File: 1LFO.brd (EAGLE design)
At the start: 96.8 x 17.8 mm, 26 parts, among them IC1 LM324D

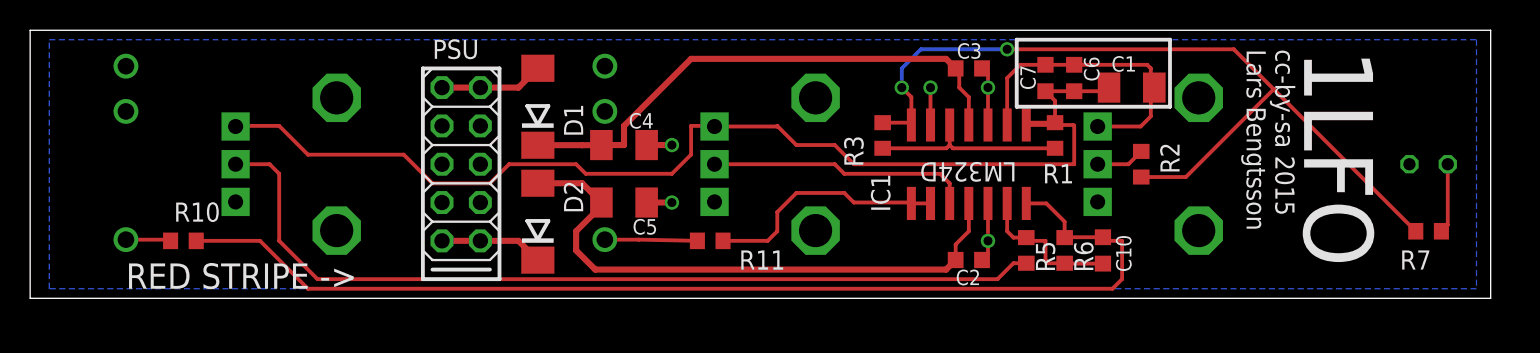
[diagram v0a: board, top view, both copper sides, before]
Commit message: Moved LED 2.54mm up, fits panel now (originally a mistake, but panel looks fine now. Better fix board). Also, size down other end of PCB to save a few cents on manufacturing.
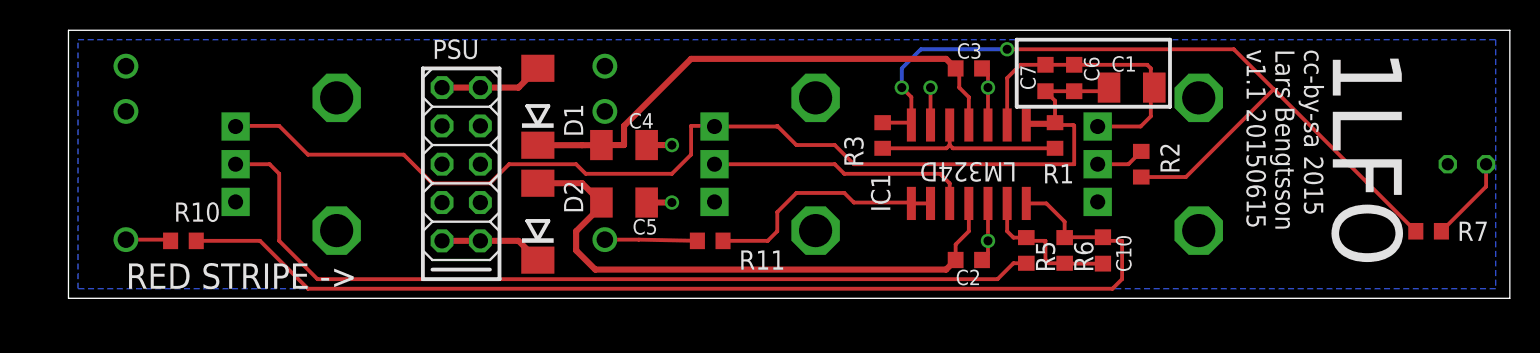
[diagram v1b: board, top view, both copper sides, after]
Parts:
- LED1: device led:LED5MM -> led:LED3MM
- moved LED1 2.54 mm to (96.5, 10.2)
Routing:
- net N$13: track 4.62 -> 5.67 mm
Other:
- board size 96.8 x 17.8 mm -> 95.6 x 17.8 mm
- board text added: "cc-by-sa 2015 Lars Bengtsson v1.1 20150615"
- board text removed: "cc-by-sa 2015 Lars Bengtsson"
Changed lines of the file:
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@@
 <board>
 <plain>
-<wire x1="1.27" y1="1.27" x2="98.095" y2="1.27" width="0" layer="20"/>
-<wire x1="98.095" y1="1.27" x2="98.095" y2="19.04" width="0" layer="20"/>
-<wire x1="98.095" y1="19.04" x2="1.27" y2="19.04" width="0" layer="20"/>
-<wire x1="1.27" y1="19.04" x2="1.27" y2="1.27" width="0" layer="20"/>
+<wire x1="3.81" y1="1.27" x2="99.365" y2="1.27" width="0" layer="20"/>
+<wire x1="99.365" y1="1.27" x2="99.365" y2="19.04" width="0" layer="20"/>
+<wire x1="99.365" y1="19.04" x2="3.81" y2="19.04" width="0" layer="20"/>
+<wire x1="3.81" y1="19.04" x2="3.81" y2="1.27" width="0" layer="20"/>
 <wire x1="27.305" y1="16.51" x2="27.305" y2="2.54" width="0.254" layer="25"/>
 <wire x1="27.305" y1="2.54" x2="32.385" y2="2.54" width="0.254" layer="25"/>
@@
 <wire x1="27.305" y1="16.51" x2="32.385" y2="16.51" width="0.254" layer="25"/>
 <text x="7.62" y="1.905" size="1.6764" layer="25" font="vector">RED STRIPE -&gt;</text>
-<text x="85.725" y="17.78" size="4.572" layer="25" font="vector" rot="SR270">1LFO</text>
+<text x="87.63" y="17.78" size="4.572" layer="25" font="vector" rot="SR270">1LFO</text>
 <text x="81.915" y="17.78" size="1.27" layer="25" font="vector" rot="SR270">cc-by-sa 2015
-Lars Bengtsson</text>
+Lars Bengtsson
+v1.1 20150615</text>
 <wire x1="66.675" y1="18.415" x2="66.675" y2="13.97" width="0.254" layer="25"/>
 <wire x1="66.675" y1="13.97" x2="76.835" y2="13.97" width="0.254" layer="25"/>
@@
 <element name="INV.AM." library="pot-alps" package="ALPS_POT_VERTICAL" value="100k" x="21.59" y="10.16" rot="MR270"/>
 <element name="OUT" library="thonkiconn" package="WQP-PJ301M-12_JACK" value="WQP-PJ301M-12_JACK" x="39.37" y="10.16" rot="MR180"/>
-<element name="INV_OUT" library="thonkiconn" package="WQP-PJ301M-12_JACK" value="WQP-PJ301M-12_JACK" x="7.62" y="10.16" rot="MR180"/>
+<element name="INV_OUT" library="thonkiconn" package="WQP-PJ301M-12_JACK" value="WQP-PJ301M-12_JACK" x="7.62" y="10.16" smashed="yes" rot="MR180">
+<attribute name="NAME" x="13.6652" y="17.1704" size="1.27" layer="22" rot="MR270"/>
+</element>
 <element name="R7" library="rcl" package="R0603" value="10k" x="93.98" y="5.715" smashed="yes">
-<attribute name="NAME" x="92.075" y="3.175" size="1.27" layer="25"/>
-<attribute name="VALUE" x="94.615" y="3.175" size="1.27" layer="27"/>
-</element>
-<element name="LED1" library="led" package="LED5MM" value="" x="93.98" y="10.16" smashed="yes" rot="MR0">
-<attribute name="NAME" x="96.52" y="13.8684" size="1.27" layer="26" ratio="10" rot="MR0"/>
-<attribute name="VALUE" x="90.7796" y="8.3566" size="1.27" layer="28" ratio="10" rot="MR0"/>
+<attribute name="NAME" x="95.885" y="5.08" size="1.27" layer="25"/>
+<attribute name="VALUE" x="95.885" y="3.175" size="1.27" layer="27"/>
+</element>
+<element name="LED1" library="led" package="LED3MM" value="" x="96.52" y="10.16" smashed="yes" rot="MR0">
+<attribute name="NAME" x="97.79" y="13.2334" size="1.27" layer="26" ratio="10" rot="MR0"/>
+<attribute name="VALUE" x="93.3196" y="8.3566" size="1.27" layer="28" ratio="10" rot="MR0"/>
 </element>
 </elements>
@@
 <contactref element="LED1" pad="K"/>
 <polygon width="0.254" layer="16" isolate="0.3048">
-<vertex x="2.54" y="18.415"/>
-<vertex x="97.155" y="18.415"/>
-<vertex x="97.155" y="1.905"/>
-<vertex x="2.54" y="1.905"/>
+<vertex x="4.445" y="18.415"/>
+<vertex x="98.425" y="18.415"/>
+<vertex x="98.425" y="1.905"/>
+<vertex x="4.445" y="1.905"/>
 </polygon>
 <wire x1="64.77" y1="12.76" x2="64.77" y2="12.7" width="0.254" layer="1"/>
@@
 <contactref element="R7" pad="2"/>
 <contactref element="LED1" pad="A"/>
-<wire x1="95.25" y1="10.16" x2="95.25" y2="6.135" width="0.254" layer="1"/>
-<wire x1="95.25" y1="6.135" x2="94.83" y2="5.715" width="0.254" layer="1"/>
+<wire x1="97.79" y1="10.16" x2="97.79" y2="8.675" width="0.254" layer="1"/>
+<wire x1="97.79" y1="8.675" x2="94.83" y2="5.715" width="0.254" layer="1"/>
 </signal>
 </signals>

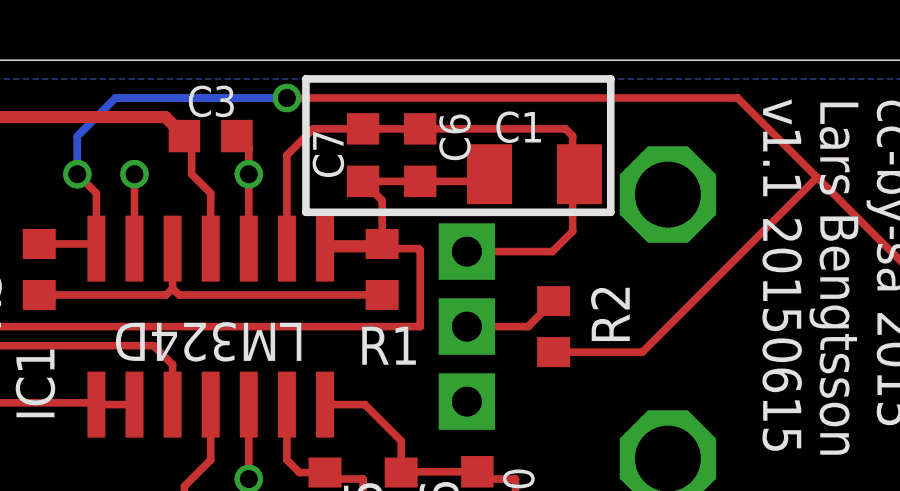
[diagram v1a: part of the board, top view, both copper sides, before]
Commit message: Removed C7. Moved remaining timing caps a bit and changed value to the right one (10uF). Only one of C1 and C6 needs to be fitted. 10uF caps are easier to find in 1206 packages with higher voltage tolerances (should be >= 16V).
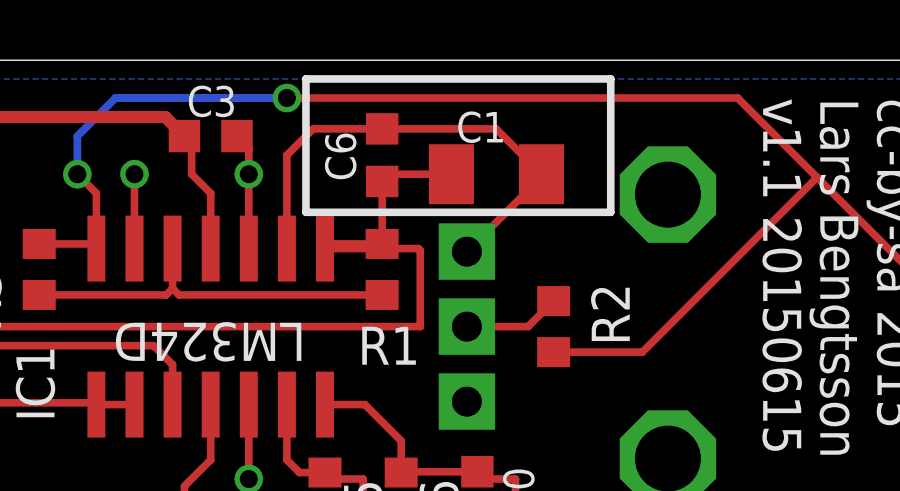
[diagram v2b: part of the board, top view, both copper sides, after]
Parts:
- removed C7: 1u, rcl:C0603K
- C1, C6: value 1u -> 10u
- moved C1 1.27 mm to (73.0, 15.2)
- moved C6 1.27 mm to (69.2, 15.9)
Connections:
- net N$1: no longer C7.1
- net TRI: no longer C7.2
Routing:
- net N$1: track 20.3 -> 16.2 mm
- net TRI: track 75.9 -> 73.7 mm
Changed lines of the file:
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@@
 </autorouter>
 <elements>
-<element name="C1" library="rcl" package="C1206K" value="1u" x="74.295" y="15.24" smashed="yes" rot="R180">
-<attribute name="NAME" x="74.625" y="17.315" size="1.016" layer="25" rot="R180"/>
+<element name="C1" library="rcl" package="C1206K" value="10u" x="73.025" y="15.24" smashed="yes" rot="R180">
+<attribute name="NAME" x="73.355" y="17.315" size="1.016" layer="25" rot="R180"/>
 <attribute name="VALUE" x="76.53" y="17.34" size="1.016" layer="27" rot="R180"/>
 </element>
@@
 <attribute name="VALUE" x="42.875" y="5.275" size="1.016" layer="27" rot="R180"/>
 </element>
-<element name="C6" library="rcl" package="C0603K" value="1u" x="70.485" y="15.875" smashed="yes" rot="R270">
-<attribute name="NAME" x="71.135" y="17.31" size="1.016" layer="25" rot="R270"/>
-<attribute name="VALUE" x="70.32" y="17.4" size="1.016" layer="27"/>
-</element>
-<element name="C7" library="rcl" package="C0603K" value="1u" x="68.58" y="15.875" smashed="yes" rot="R270">
-<attribute name="NAME" x="67.93" y="15.075" size="1.016" layer="25" rot="R90"/>
+<element name="C6" library="rcl" package="C0603K" value="10u" x="69.215" y="15.875" smashed="yes" rot="R270">
+<attribute name="NAME" x="67.325" y="16.675" size="1.016" layer="25" rot="R270"/>
 <attribute name="VALUE" x="67.78" y="17.4" size="1.016" layer="27"/>
 </element>
@@
 <contactref element="C1" pad="1"/>
 <contactref element="C6" pad="1"/>
-<contactref element="C7" pad="1"/>
-<wire x1="68.58" y1="16.75" x2="70.485" y2="16.75" width="0.254" layer="1"/>
-<wire x1="68.58" y1="16.75" x2="66.915" y2="16.75" width="0.254" layer="1"/>
 <wire x1="66.915" y1="16.75" x2="66.04" y2="15.875" width="0.254" layer="1"/>
 <wire x1="66.04" y1="15.875" x2="66.04" y2="12.76" width="0.254" layer="1"/>
-<wire x1="70.485" y1="16.75" x2="75.325" y2="16.75" width="0.254" layer="1"/>
-<wire x1="75.325" y1="16.75" x2="75.565" y2="16.51" width="0.254" layer="1"/>
-<wire x1="75.565" y1="16.51" x2="75.565" y2="15.47" width="0.254" layer="1"/>
-<wire x1="75.565" y1="15.47" x2="75.795" y2="15.24" width="0.254" layer="1"/>
-<wire x1="72.04" y1="12.66" x2="74.89" y2="12.66" width="0.254" layer="1"/>
-<wire x1="74.89" y1="12.66" x2="75.565" y2="13.335" width="0.254" layer="1"/>
-<wire x1="75.565" y1="13.335" x2="75.565" y2="15.01" width="0.254" layer="1"/>
-<wire x1="75.565" y1="15.01" x2="75.795" y2="15.24" width="0.254" layer="1"/>
+<wire x1="66.915" y1="16.75" x2="69.215" y2="16.75" width="0.254" layer="1"/>
+<wire x1="69.215" y1="16.75" x2="73.015" y2="16.75" width="0.254" layer="1"/>
+<wire x1="73.015" y1="16.75" x2="74.525" y2="15.24" width="0.254" layer="1"/>
+<wire x1="74.525" y1="15.24" x2="74.525" y2="15.145" width="0.254" layer="1"/>
+<wire x1="74.525" y1="15.145" x2="72.04" y2="12.66" width="0.254" layer="1"/>
 </signal>
 <signal name="TRI">
@@
 <contactref element="C1" pad="2"/>
 <contactref element="C6" pad="2"/>
-<contactref element="C7" pad="2"/>
 <contactref element="AM." pad="P$1"/>
 <contactref element="INV.AM." pad="P$1"/>
 <wire x1="69.215" y1="12.915" x2="67.465" y2="12.915" width="0.254" layer="1"/>
 <wire x1="67.465" y1="12.915" x2="67.31" y2="12.76" width="0.254" layer="1"/>
-<wire x1="69.215" y1="12.915" x2="69.215" y2="14.365" width="0.254" layer="1"/>
-<wire x1="69.215" y1="14.365" x2="68.58" y2="15" width="0.254" layer="1"/>
-<wire x1="68.58" y1="15" x2="70.485" y2="15" width="0.254" layer="1"/>
-<wire x1="70.485" y1="15" x2="72.555" y2="15" width="0.254" layer="1"/>
-<wire x1="72.555" y1="15" x2="72.795" y2="15.24" width="0.254" layer="1"/>
+<wire x1="69.215" y1="12.915" x2="69.215" y2="15" width="0.254" layer="1"/>
 <wire x1="67.31" y1="12.76" x2="70.425" y2="12.76" width="0.254" layer="1"/>
 <wire x1="70.425" y1="12.76" x2="70.485" y2="12.7" width="0.254" layer="1"/>
@@
 <wire x1="50.8" y1="12.7" x2="52.07" y2="11.43" width="0.254" layer="1"/>
 <wire x1="52.07" y1="11.43" x2="54.61" y2="11.43" width="0.254" layer="1"/>
+<wire x1="71.525" y1="15.24" x2="69.455" y2="15.24" width="0.254" layer="1"/>
+<wire x1="69.455" y1="15.24" x2="69.215" y2="15" width="0.254" layer="1"/>
 </signal>
 <signal name="N$5">
